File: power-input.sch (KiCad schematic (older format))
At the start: 17 parts, among them J301 Conn_01x02, J302 Conn_01x02, J303 Conn_01x02, U301 SY8401

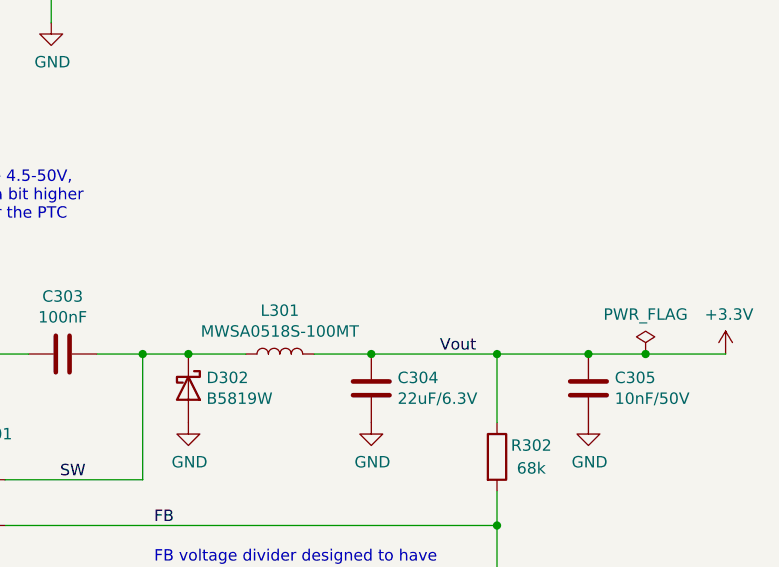
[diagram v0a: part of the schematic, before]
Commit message: Change buck converter inductor to something available at JLCPCB
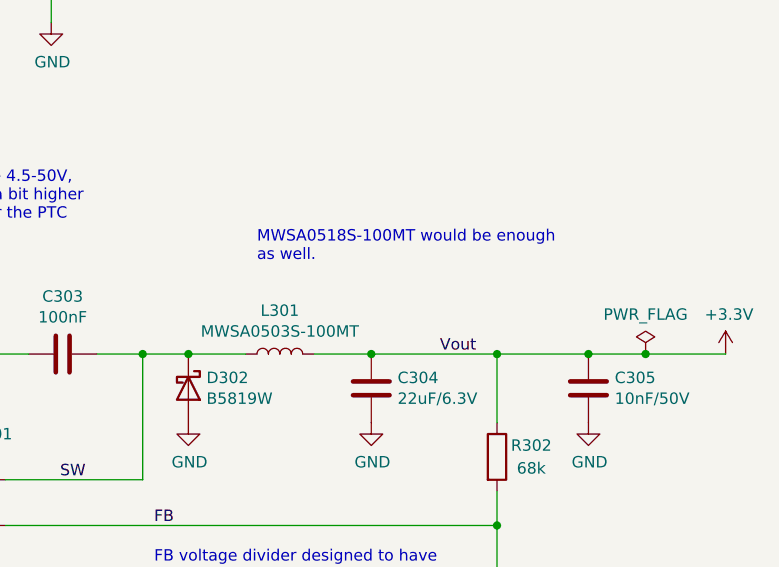
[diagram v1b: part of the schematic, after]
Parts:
- L301: value MWSA0518S-100MT -> MWSA0503S-100MT; LCSC C408349 -> C408412
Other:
- note added: "MWSA0518S-100MT would be enough\nas well."
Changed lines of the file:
@@
 AR Path="/5F6FAF6E/5CA62D7A" Ref="L301"  Part="1"
 F 0 "L301" V 6590 4250 50  0000 C CNN
-F 1 "MWSA0518S-100MT" V 6499 4250 50  0000 C CNN
+F 1 "MWSA0503S-100MT" V 6499 4250 50  0000 C CNN
 F 2 "Inductor_SMD:L_Sunlord_MWSA0518_5.4x5.2mm" H 6400 4250 50  0001 C CNN
 F 3 "~" H 6400 4250 50  0001 C CNN
 F 4 "" V 6400 4250 50  0001 C CNN "URL"
 F 5 "" V 6400 4250 50  0001 C CNN "Part"
-F 6 "C408349" H 6400 4250 50  0001 C CNN "LCSC"
+F 6 "C408412" H 6400 4250 50  0001 C CNN "LCSC"
 	1    6400 4250
 	0    -1   -1   0
@@
 Wire Wire Line
 	1600 1400 6500 1400
+Text Notes 6300 3850 0    50   ~ 0
+MWSA0518S-100MT would be enough\nas well.
 $EndSCHEMATC

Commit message: Switch power and  NEMA to JST-XH Connectors and update silkscreen accordingly
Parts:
- J301: footprint Connector_Phoenix_MC:PhoenixContact_MCV_1,5_2-G-3.81_1x02_P3.81mm_Vertical -> Connector_JST:JST_XH_B2B-XH-A_1x02_P2.50mm_Vertical
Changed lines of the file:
@@
 F 0 "J301" H 1750 2300 50  0000 C CNN
 F 1 "Conn_01x02" H 1750 2200 50  0000 C CNN
-F 2 "Connector_Phoenix_MC:PhoenixContact_MCV_1,5_2-G-3.81_1x02_P3.81mm_Vertical" H 1750 2100 50  0001 C CNN
+F 2 "Connector_JST:JST_XH_B2B-XH-A_1x02_P2.50mm_Vertical" H 1750 2100 50  0001 C CNN
 F 3 "~" H 1750 2100 50  0001 C CNN
 F 4 "C8396" H 1750 2100 50  0001 C CNN "LCSC"

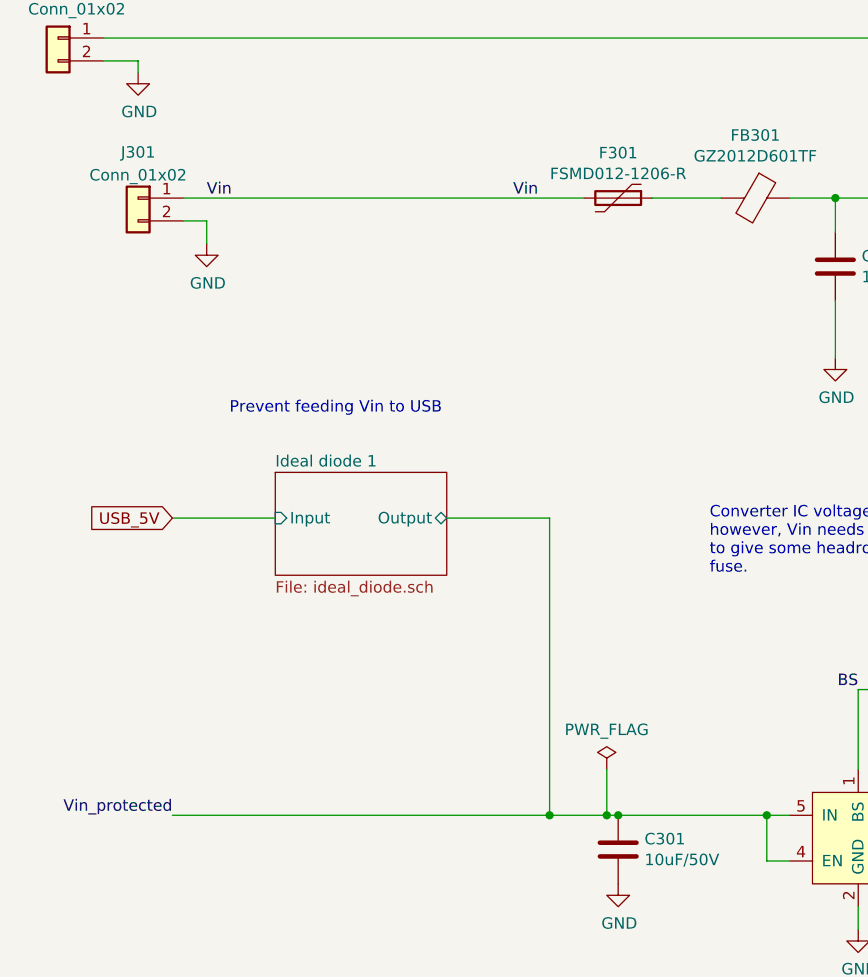
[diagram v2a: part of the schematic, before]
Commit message: Power system bug fix. Changed fuses & Diode - Swapping incorrect part  D1101 and D1102  to BAT54A   /  LCSC:  C83936 -Removed Perfect Diode, replaced with B5819W  Schottky - Replaced USB PTC Fuse ( F401 ) with   ASMD1206-050  /   C135338 - Replaced VIN ( F301 ) & CAN (F601 )PTC Fuses with  mSMD050-60V  / C70113 - Rerouted power and CAN power areas of board. - Removed all perfectDiode components/tracks and replaced with Schottky
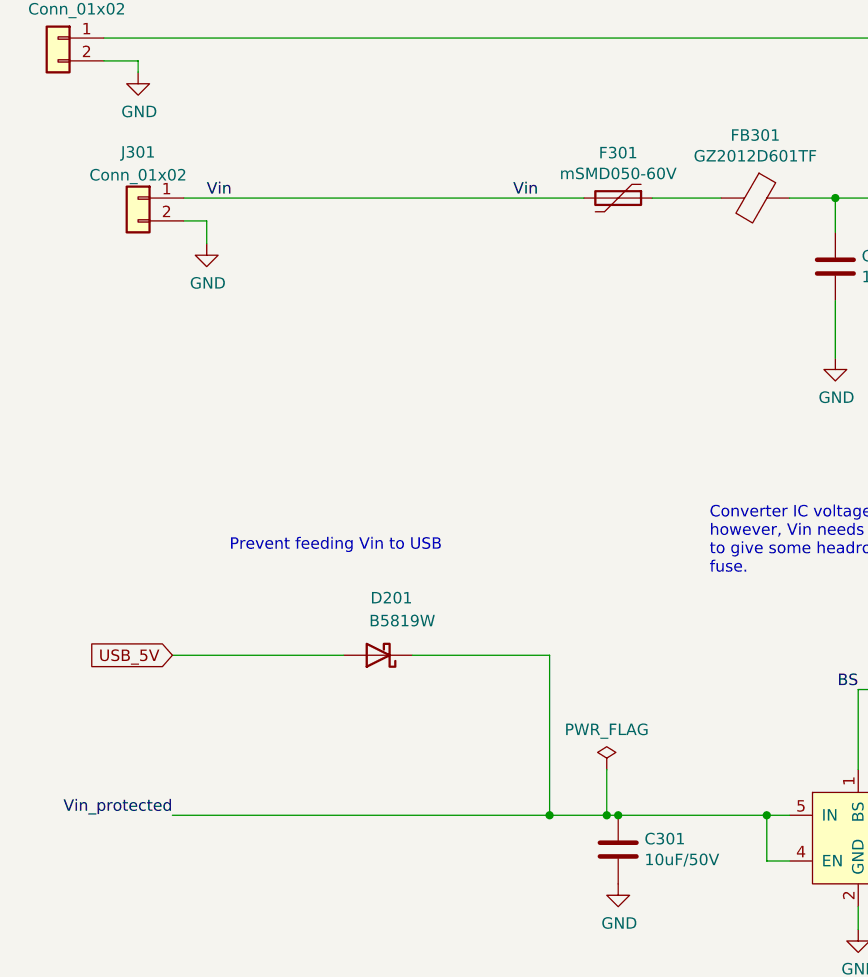
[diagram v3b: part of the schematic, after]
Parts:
- added D201: B5819W, Diode_SMD:D_SOD-123, symbol Device:D_Schottky
- F301: value FSMD012-1206-R -> mSMD050-60V; footprint Fuse:Fuse_1206_3216Metric -> Fuse:Fuse_1812_4532Metric; LCSC C220144 -> C70113
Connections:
- net USB_5V: now also D201.2 (A)
- net Vin_protected: now also D201.1 (K)
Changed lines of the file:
@@
 $Descr A4 11693 8268
 encoding utf-8
-Sheet 2 11
+Sheet 2 10
 Title "Sailor Hat for ESP32"
 Date "2020-11-25"
@@
 AR Path="/5F6FAF6E/5E467AC2" Ref="F301"  Part="1"
 F 0 "F301" V 3653 2100 50  0000 C CNN
-F 1 "FSMD012-1206-R" V 3744 2100 50  0000 C CNN
-F 2 "Fuse:Fuse_1206_3216Metric" V 3780 2100 50  0001 C CNN
+F 1 "mSMD050-60V" V 3744 2100 50  0000 C CNN
+F 2 "Fuse:Fuse_1812_4532Metric" V 3780 2100 50  0001 C CNN
 F 3 "~" H 3850 2100 50  0001 C CNN
-F 4 "C220144" H 3850 2100 50  0001 C CNN "LCSC"
+F 4 "C70113" H 3850 2100 50  0001 C CNN "LCSC"
 	1    3850 2100
 	0    1    1    0
@@
 Wire Wire Line
 	3800 4800 3850 4800
-Text GLabel 1900 3500 0    50   Input ~ 0
+Text GLabel 1900 4100 0    50   Input ~ 0
 USB_5V
 Text Notes 4250 3750 0    50   ~ 0
@@
 CAN12V_Prot
 Wire Wire Line
-	3550 3500 3550 4800
-$Sheet
-S 2350 3300 750  450
-U 5FBC3428
-F0 "Ideal diode 1" 50
-F1 "ideal_diode.sch" 50
-F2 "Input" I L 2350 3500 50
-F3 "Output" B R 3100 3500 50
-$EndSheet
-Wire Wire Line
-	3550 3500 3100 3500
-Wire Wire Line
-	2350 3500 1900 3500
+	3550 4100 3550 4800
 Connection ~ 5750 2100
 Wire Wire Line
 	1900 4800 3550 4800
-Text Notes 2150 3050 0    50   ~ 0
+Text Notes 2150 3650 0    50   ~ 0
 Prevent feeding Vin to USB
 $Comp
@@
 Text Notes 6300 3850 0    50   ~ 0
 MWSA0518S-100MT would be enough\nas well.
+$Comp
+L Device:D_Schottky D?
+U 1 1 5FF3661F
+P 2800 4100
+AR Path="/5C3476D8/5FF3661F" Ref="D?"  Part="1"
+AR Path="/5CA65CC5/5FF3661F" Ref="D?"  Part="1"
+AR Path="/5F6FAF6E/5FF3661F" Ref="D201"  Part="1"
+F 0 "D201" H 2650 3850 50  0000 L CNN
+F 1 "B5819W" H 2550 3950 50  0000 L CNN
+F 2 "Diode_SMD:D_SOD-123" H 2800 4100 50  0001 C CNN
+F 3 "~" H 2800 4100 50  0001 C CNN
+F 4 "" V 2800 4100 50  0001 C CNN "Notes"
+F 5 "C8598" H 2800 4100 50  0001 C CNN "LCSC"
+	1    2800 4100
+	-1   0    0    1
+$EndComp
+Wire Wire Line
+	1900 4100 2650 4100
+Wire Wire Line
+	2950 4100 3550 4100
 $EndSCHEMATC

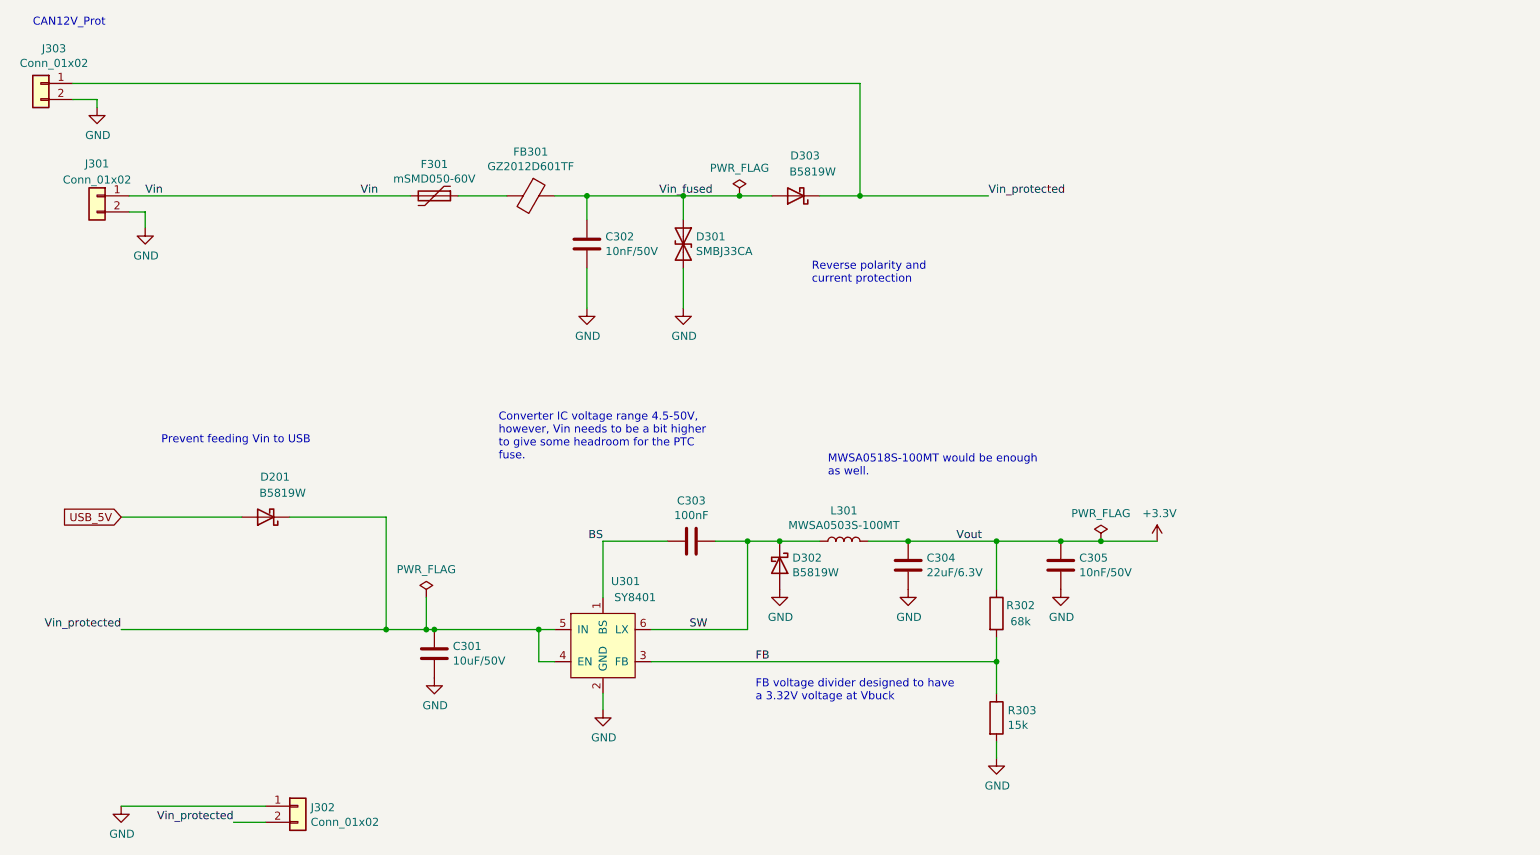
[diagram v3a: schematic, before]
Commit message: Add an LC pi filter to buck converter input
The filter is required to limit conducted noise emissions.
Additionally, buck inductor is changed and the whole SMPS region
is rearranged. Update title block data.
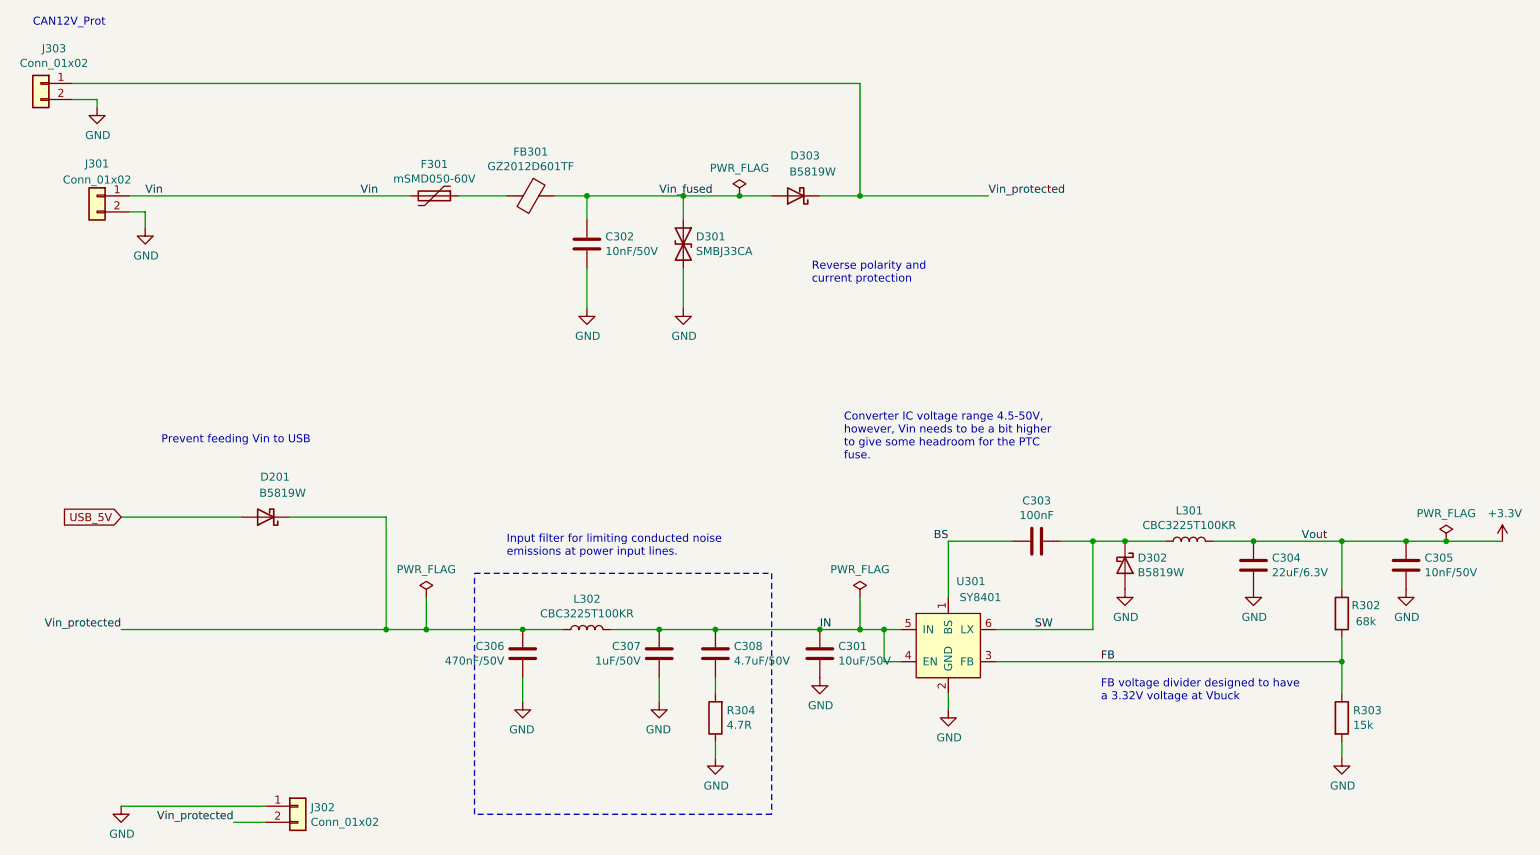
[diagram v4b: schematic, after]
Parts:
- added C306: 470nF/50V, Capacitor_SMD:C_0805_2012Metric, symbol Device:C
- added C307: 1uF/50V, Capacitor_SMD:C_0805_2012Metric, symbol Device:C
- added C308: 4.7uF/50V, Capacitor_SMD:C_1206_3216Metric, symbol Device:C
- added L302: CBC3225T100KR, Inductor_SMD:L_1210_3225Metric, symbol Device:L
- added R304: 4.7R, Resistor_SMD:R_0603_1608Metric, symbol Device:R
- L301: value MWSA0503S-100MT -> CBC3225T100KR; footprint Inductor_SMD:L_Sunlord_MWSA0518_5.4x5.2mm -> Inductor_SMD:L_1210_3225Metric; LCSC C408412 -> C90321
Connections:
- net GND: now also C306.1, C307.1, R304.1
- net Vin_protected: now also C306.2, L302.1; no longer C301.1, U301.4 (EN), U301.5 (IN)
- new net: C308.2, R304.2
- new net IN: C301.1, C307.2, C308.1, L302.2, U301.4 (EN), U301.5 (IN)
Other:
- note added: "Input filter for limiting conducted noise \nemissions at power input lines."
- note removed: "MWSA0518S-100MT would be enough\nas well."
- moved on the sheet: C301, C303, C304, C305, D302, L301, R302, R303, U301

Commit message: Update parts according to JLC availability
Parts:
- D301: LCSC C143164 -> C114000
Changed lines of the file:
@@
 F 2 "Diode_SMD:D_SMB" H 5400 2400 50  0001 C CNN
 F 3 "~" H 5400 2400 50  0001 C CNN
-F 4 "C143164" H 5400 2400 50  0001 C CNN "LCSC"
+F 4 "C114000" H 5400 2400 50  0001 C CNN "LCSC"
 	1    5400 2400
 	0    1    1    0

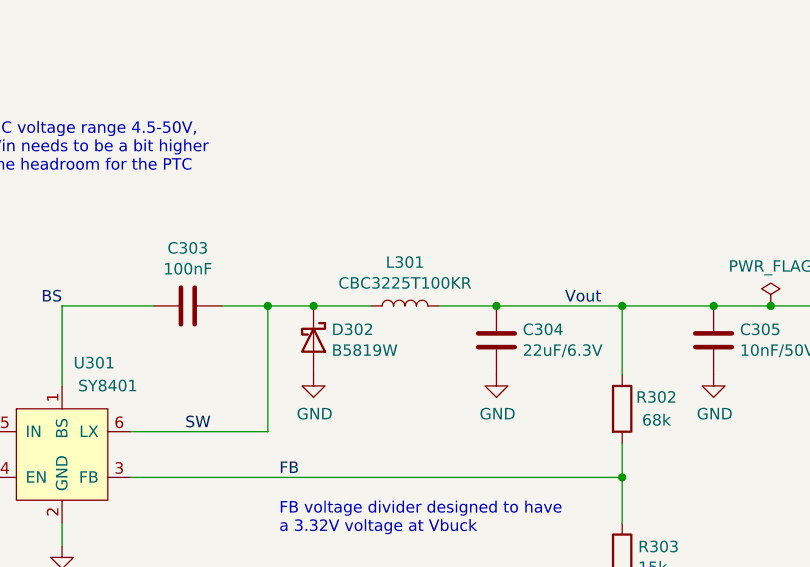
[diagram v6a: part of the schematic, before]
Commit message: Change the buck converter inductor back to a shielded one
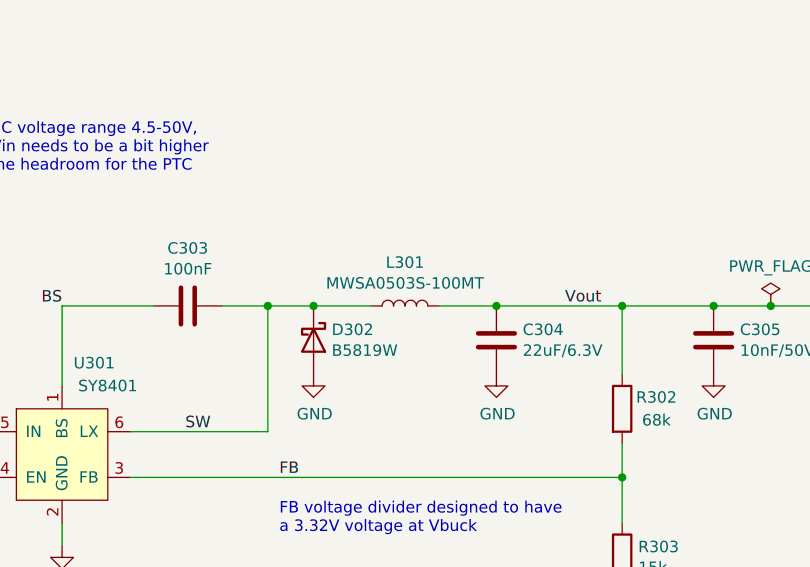
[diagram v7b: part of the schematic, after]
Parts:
- L301: value CBC3225T100KR -> MWSA0503S-100MT; footprint Inductor_SMD:L_1210_3225Metric -> Inductor_SMD:L_Sunlord_MWSA0518_5.4x5.2mm; LCSC C90321 -> C408412
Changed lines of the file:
@@
 AR Path="/5F6FAF6E/5CA62D7A" Ref="L301"  Part="1"
 F 0 "L301" V 8740 4250 50  0000 C CNN
-F 1 "CBC3225T100KR" V 8649 4250 50  0000 C CNN
-F 2 "Inductor_SMD:L_1210_3225Metric" H 8550 4250 50  0001 C CNN
+F 1 "MWSA0503S-100MT" V 8649 4250 50  0000 C CNN
+F 2 "Inductor_SMD:L_Sunlord_MWSA0518_5.4x5.2mm" H 8550 4250 50  0001 C CNN
 F 3 "~" H 8550 4250 50  0001 C CNN
 F 4 "" V 8550 4250 50  0001 C CNN "URL"
 F 5 "" V 8550 4250 50  0001 C CNN "Part"
-F 6 "C90321" H 8550 4250 50  0001 C CNN "LCSC"
+F 6 "C408412" H 8550 4250 50  0001 C CNN "LCSC"
 	1    8550 4250
 	0    -1   -1   0

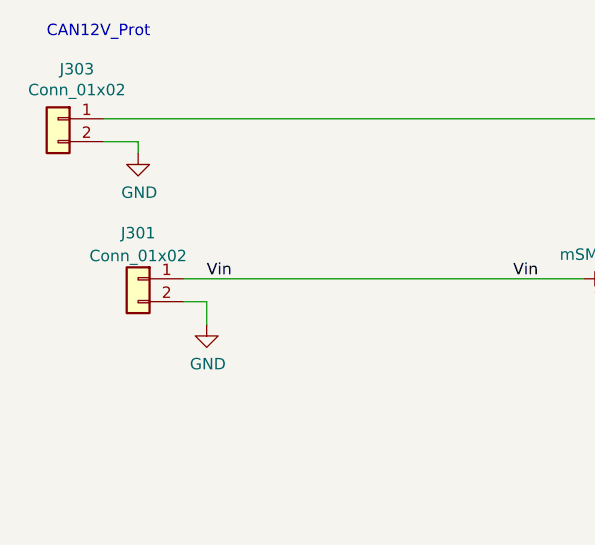
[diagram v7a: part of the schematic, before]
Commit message: Swap Power and CAN connector pins to have GND on pin 1
This complies e.g. with all pre-made pigtails.
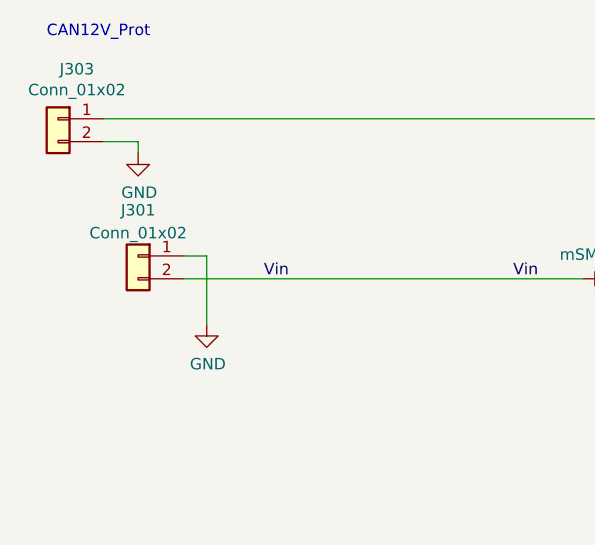
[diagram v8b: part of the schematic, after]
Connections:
- net GND: now also J301.1 (Pin_1); no longer J301.2 (Pin_2)
- net Vin: now also J301.2 (Pin_2); no longer J301.1 (Pin_1)
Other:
- moved on the sheet: J301
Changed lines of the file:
@@
 Wire Wire Line
 	3550 4800 3800 4800
-Wire Wire Line
-	2050 2200 1950 2200
-Wire Wire Line
-	2050 2300 2050 2200
-$Comp
-L power:GND #PWR?
-U 1 1 5F8B7EDA
-P 2050 2300
-AR Path="/5F8B7EDA" Ref="#PWR?"  Part="1"
-AR Path="/5C3476D8/5F8B7EDA" Ref="#PWR?"  Part="1"
-AR Path="/5E460E30/5F8B7EDA" Ref="#PWR?"  Part="1"
-AR Path="/5F6FAF6E/5F8B7EDA" Ref="#PWR0311"  Part="1"
-F 0 "#PWR0311" H 2050 2050 50  0001 C CNN
-F 1 "GND" H 2055 2127 50  0000 C CNN
-F 2 "" H 2050 2300 50  0001 C CNN
-F 3 "" H 2050 2300 50  0001 C CNN
-	1    2050 2300
-	1    0    0    -1
-$EndComp
 $Comp
 L Connector_Generic:Conn_01x02 J301
 U 1 1 5F8B6C12
-P 1750 2100
-F 0 "J301" H 1750 2300 50  0000 C CNN
-F 1 "Conn_01x02" H 1750 2200 50  0000 C CNN
-F 2 "Connector_JST:JST_XH_B2B-XH-A_1x02_P2.50mm_Vertical" H 1750 2100 50  0001 C CNN
-F 3 "~" H 1750 2100 50  0001 C CNN
-F 4 "C8396" H 1750 2100 50  0001 C CNN "LCSC"
-	1    1750 2100
+P 1750 2000
+F 0 "J301" H 1750 2200 50  0000 C CNN
+F 1 "Conn_01x02" H 1750 2100 50  0000 C CNN
+F 2 "Connector_JST:JST_XH_B2B-XH-A_1x02_P2.50mm_Vertical" H 1750 2000 50  0001 C CNN
+F 3 "~" H 1750 2000 50  0001 C CNN
+F 4 "C8396" H 1750 2000 50  0001 C CNN "LCSC"
+	1    1750 2000
 	-1   0    0    -1
 $EndComp
 Text Label 3500 2100 2    50   ~ 0
 Vin
-Text Label 2050 2100 0    50   ~ 0
+Text Label 2300 2100 0    50   ~ 0
 Vin
 $Comp
@@
 Wire Wire Line
 	6250 2100 6500 2100
-Wire Wire Line
-	1950 2100 3700 2100
 Wire Wire Line
 	6500 1400 6500 2100
@@
 Text Label 6250 4800 0    50   ~ 0
 IN
+Wire Wire Line
+	1950 2100 3700 2100
+$Comp
+L power:GND #PWR?
+U 1 1 5F8B7EDA
+P 2050 2300
+AR Path="/5F8B7EDA" Ref="#PWR?"  Part="1"
+AR Path="/5C3476D8/5F8B7EDA" Ref="#PWR?"  Part="1"
+AR Path="/5E460E30/5F8B7EDA" Ref="#PWR?"  Part="1"
+AR Path="/5F6FAF6E/5F8B7EDA" Ref="#PWR0311"  Part="1"
+F 0 "#PWR0311" H 2050 2050 50  0001 C CNN
+F 1 "GND" H 2055 2127 50  0000 C CNN
+F 2 "" H 2050 2300 50  0001 C CNN
+F 3 "" H 2050 2300 50  0001 C CNN
+	1    2050 2300
+	1    0    0    -1
+$EndComp
+Wire Wire Line
+	2050 2300 2050 2000
+Wire Wire Line
+	2050 2000 1950 2000
 $EndSCHEMATC
